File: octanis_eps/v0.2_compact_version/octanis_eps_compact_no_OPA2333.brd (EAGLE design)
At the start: 61.9 x 49.5 mm, 90 parts, among them IC3 OPA2333DGK, IC5 OPA2333DGK, IC6 OPA2333DGK, IC7 OPA2333DGK, IC9 OPA2333DGK, Q1 FC-12M, Q2 N-HEXFET-2D_SOT232-, Q3 N-HEXFET-2D_SOT232-, Q4 N-HEXFET-2D_SOT232-

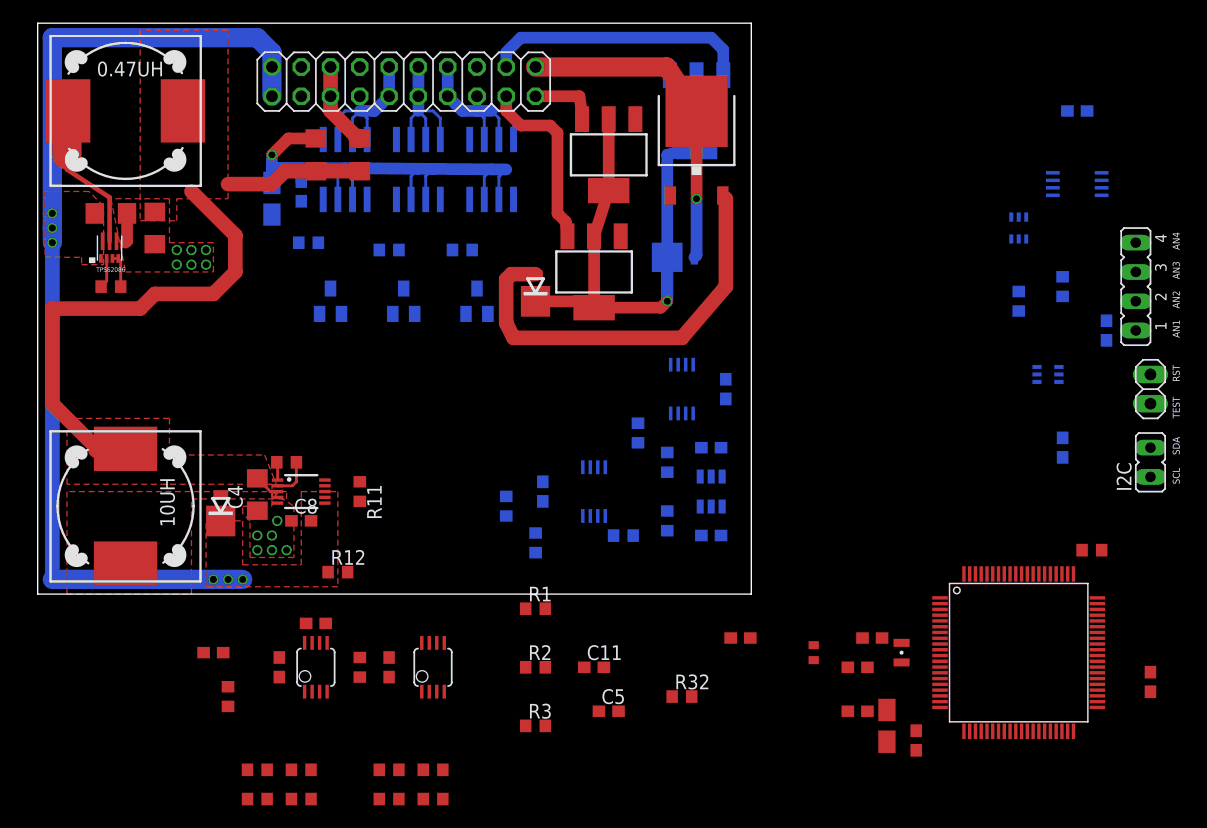
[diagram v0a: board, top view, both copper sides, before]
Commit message: compact version 5X6cm with MSP420Gxx24
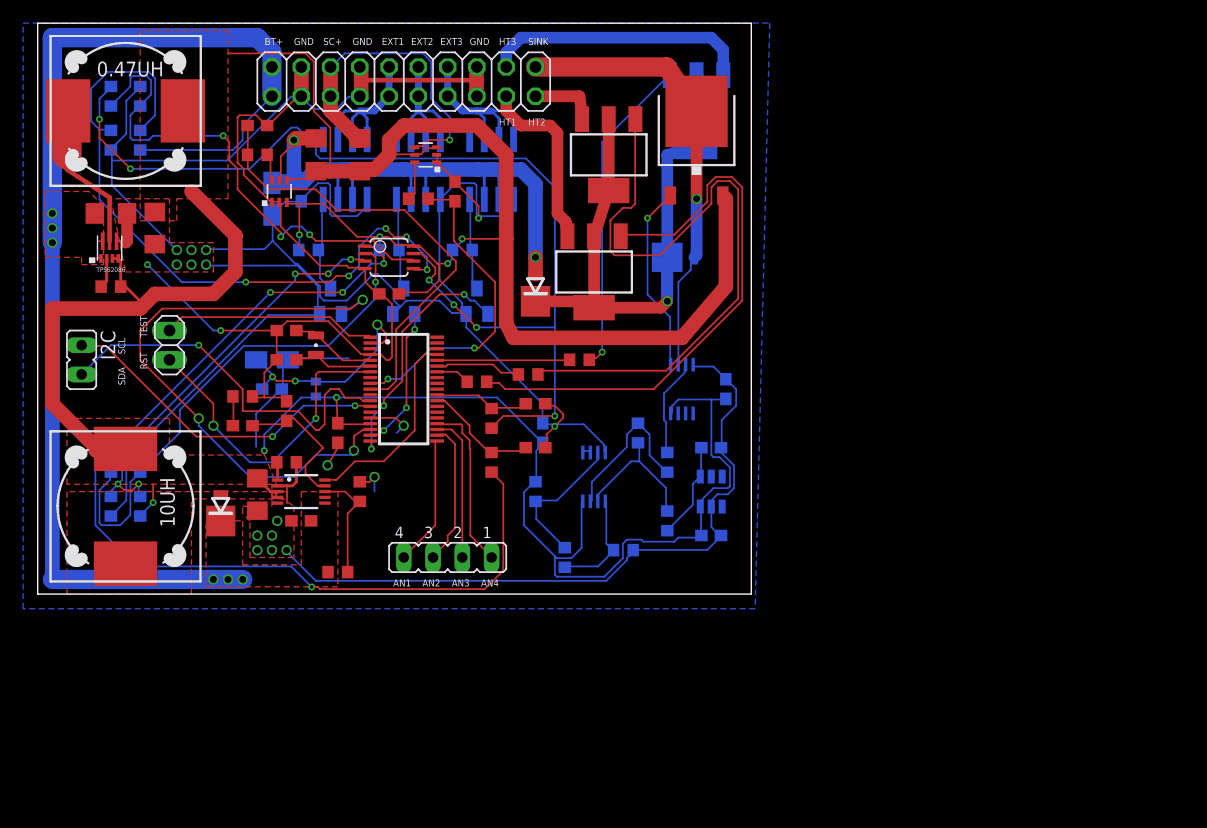
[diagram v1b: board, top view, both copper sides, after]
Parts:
- removed C20: 470nF, rcl:C0603
- removed C23, C_IC3, C_IC6: 100nF, rcl:C0603
- removed IC3, IC6: OPA2333DGK, linear:MSOP08
- removed R48: 1M, rcl:R0603
- removed U$1: F552X---PN80, TI_MSP430_v16:PN80
- added U$6: MSP430G2544, Octanis1_EPS:TSSOP38
- moved I2C 93.1 mm to (3.81, 50.8), turned to 180 degrees
- moved JP7 85.2 mm to (11.4, 52.1), turned to 90 degrees
- moved C2 75.8 mm to (19.1, 71.1), flipped to the top, turned to 180 degrees
- moved R7 67.3 mm to (19.1, 68.6), flipped to the top, turned to 0 degrees
- moved R22 64.7 mm to (8.89, 73.7), flipped to the bottom, turned to 90 degrees
- moved U$2 64.2 mm to (21.0, 65.4), flipped to the top, turned to 0 degrees
- moved A_EXT 64.1 mm to (35.6, 33.7), turned to 180 degrees
- moved R23 63.2 mm to (6.35, 73.7), flipped to the bottom, turned to 270 degrees
- moved R19 62.5 mm to (8.89, 69.8), flipped to the bottom, turned to 270 degrees
- moved C24 62.1 mm to (20.3, 50.8), flipped to the bottom, turned to 0 degrees
- moved R20 61.3 mm to (6.35, 69.8), flipped to the bottom, turned to 90 degrees
- moved C22 58.0 mm to (20.3, 48.3), flipped to the bottom
- moved C14 57.4 mm to (21.6, 53.3)
- moved Q1 57.4 mm to (24.1, 52.1)
- moved U$3 57.2 mm to (33.7, 68.6), flipped to the top
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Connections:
- removed net 65: U$1.65
- removed net 66: U$1.66
- removed net 67: U$1.67
- removed net AEXT4: A_EXT.1, U$1.80
- removed net N$11: C6.2, IC5.5, R16.1
- removed net N$27: R48.2, U$1.63
- removed net N$28: U$1.45
- removed net N$49: C20.1, U$1.20
- removed net N$6: C2.2, IC3.3, R7.1
- removed net N$7: C3.2, IC3.5, R9.1
- removed net N$9: C7.2, IC6.5, R21.1
- new net A_EXT4: A_EXT.1, U$6.23
- net +3V3: now also FERRITE_BEAD.1, U$6.2; no longer C21.2, C23.1, FERRITE_BEAD.2, U$1.14, U$1.18, U$1.50
- net A_EXT1: now also U$6.20; no longer U$1.77
- net A_EXT2: now also U$6.21; no longer U$1.78
- net A_EXT3: now also U$6.22; no longer U$1.79
- net EN_CHG: now also U$6.35; no longer U$1.29
- net EN_EXT1: now also U$6.17; no longer U$1.31
- net EN_EXT2: now also U$6.18; no longer U$1.32
- net EN_EXT3: now also U$6.19; no longer U$1.33
- net EN_HEAT1: now also U$6.32; no longer U$1.34
- net EN_HEAT2: now also U$6.33; no longer U$1.35
- net EN_HEAT3: now also U$6.34; no longer U$1.36
- net EXT_PW: now also U$8.A
- net GND: now also C21.1, U$6.15, U$6.4; no longer C20.2, C23.2, C_IC3.1, C_IC6.1, IC3.4, IC6.4, R48.1, U$1.19, U$1.49, U$1.61, U$1.68
- net I2C_SCL: now also U$6.13; no longer U$1.47
- net I2C_SDA: now also U$6.12; no longer U$1.46
- net I_EXT_PW: now also C2.2, R7.1, U$6.10; no longer IC3.1, IC3.2, U$1.6
- net I_SC: now also C3.2, R9.1, U$6.9; no longer IC3.6, IC3.7, U$1.5
- net N$10: now also IC5.7; no longer IC6.1
- net N$15: now also IC5.6; no longer IC6.2
- net N$16: now also IC5.5; no longer IC6.3
- net N$48: now also U$6.5; no longer U$1.12
- net N$50: now also U$6.6; no longer U$1.13
- net RST/SBWTDIO: now also U$6.7; no longer U$1.76
- net TEST/SBWTCK: now also U$6.1; no longer U$1.71
- net VCC: now also C21.2, FERRITE_BEAD.2, U$6.16; no longer C21.1, C_IC3.2, C_IC6.2, FERRITE_BEAD.1, IC3.8, IC6.8, U$1.11, U$8.A
- net V_BT_MS: now also C7.2, R21.1, U$6.28; no longer IC6.6, IC6.7, U$1.2
- net V_BUS_MS: now also C6.2, R16.1, U$6.27; no longer IC5.6, IC5.7, U$1.1
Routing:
- net GND: track 6.06 -> 363.5 mm, vias 12 -> 19
- net VCC: track 95.6 -> 266.4 mm, vias 0 -> 7
- net N$10: track 0.00 -> 91.6 mm, vias 0 -> 6
- net N$12: track 0.00 -> 87.3 mm, vias 0 -> 4
- net N$16: track 0.00 -> 59.9 mm, vias 0 -> 5
- net N$31: track 0.00 -> 57.5 mm
- net EN_EXT1: track 0.00 -> 52.2 mm, vias 0 -> 3
- net N$29: track 0.00 -> 49.5 mm
- net N$13: track 0.00 -> 44.5 mm, vias 0 -> 1
- net N$15: track 0.00 -> 43.1 mm, vias 0 -> 3
- net I_EXT_PW: track 0.00 -> 40.2 mm
- net N$14: track 0.00 -> 36.0 mm, vias 0 -> 5
- net I2C_SDA: track 0.00 -> 33.8 mm, vias 0 -> 1
- net I2C_SCL: track 0.00 -> 29.4 mm, vias 0 -> 2
- net I_SC: track 0.00 -> 27.9 mm, vias 0 -> 2
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- added copper zone on layer 16, net GND
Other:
- board text added: "BT+"
- board text added: "EXT1"
- board text added: "EXT2"
- board text added: "EXT3"
- board text added: "GND"
- board text added: "HT1"
- board text added: "HT2"
- board text added: "HT3"
- board text added: "SC+"
- board text added: "SINK"

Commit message: correction & redesign on of the boost converter running
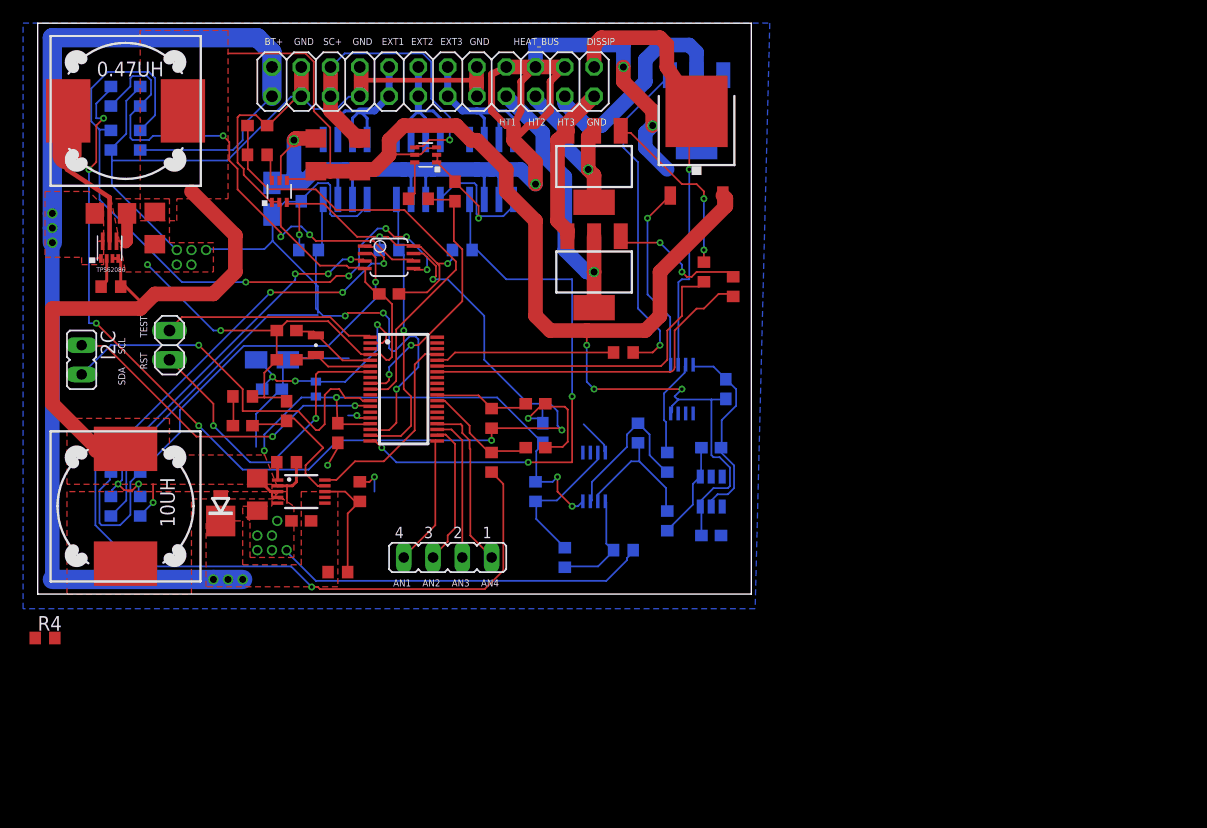
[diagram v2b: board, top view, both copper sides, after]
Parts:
- removed U$13, U$14, U$15: FDV301N, Octanis1_EPS:SOT23
- removed U$8, U$9: MBRM120LTIG, Octanis1_EPS:DO216AA
- added R4: 100k, rcl:R0603
- C2, C3, C6, C7: value 150nF -> 1.5uF
- JP1: device pinhead:2X10 -> pinhead:2X12
- R11: value 549k -> 50k
- R12: value 1.3M -> 286k
- R16, R21, R7, R9: value 10k -> 1k
- moved R1 23.7 mm to (60.3, 57.1), turned to 270 degrees
- moved R2 17.6 mm to (57.8, 58.4), turned to 270 degrees
- moved R3 3.86 mm to (50.8, 51.4)
- moved JP1 2.54 mm to (34.3, 74.9)
- moved Q3 1.63 mm to (48.3, 67.6)
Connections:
- removed net N$17: IC7.1, IC7.2
- removed net N$34: R80.2, U$15.3, U$17.4
- removed net N$79: R81.2, U$13.3, U$16.4
- removed net N$80: R79.2, U$14.3, U$18.4
- net DISSIP: now also JP1.24; no longer JP1.20, U$9.A
- net EN_EXT1: now also R81.2, U$16.4; no longer U$13.1
- net EN_EXT2: now also R80.2, U$17.4; no longer U$15.1
- net EN_EXT3: now also R79.2, U$18.4; no longer U$14.1
- net EXT_PW: now also JP1.18, JP1.20, JP1.22; no longer U$8.A
- net GND: now also JP1.23, Q2.3, Q3.3, Q4.3; no longer U$13.2, U$14.2, U$15.2
- net HEAT1: now also Q2.2, Q2.4; no longer Q2.3
- net HEAT2: now also Q3.2, Q3.4; no longer Q3.3
- net HEAT3: now also JP1.21, Q4.2, Q4.4; no longer JP1.18, Q4.3
- net N$18: no longer IC7.3
- net N$23: now also R4.1
- net N$5: now also R4.2; no longer Q2.2, Q2.4, Q3.2, Q3.4, Q4.2, Q4.4, U$8.C, U$9.C
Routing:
- net N$5: track 53.8 -> 0.00 mm, vias 1 -> 0
- net GND: track 363.5 -> 315.1 mm, vias 19 -> 18
- net EXT_PW: track 58.7 -> 105.6 mm, vias 2 -> 4
- net N$31: track 57.5 -> 15.5 mm, vias 0 -> 2
- net N$29: track 49.5 -> 11.9 mm, vias 0 -> 2
- net EN_HEAT1: track 2.96 -> 30.4 mm
- net EN_EXT3: track 21.6 -> 48.4 mm
- net VCC: track 266.4 -> 244.6 mm, vias 7 -> 11
- net EN_HEAT2: track 7.55 -> 29.1 mm
- net EN_EXT1: track 52.2 -> 33.1 mm
- net EN_EXT2: track 12.6 -> 24.1 mm, vias 3 -> 1
- net HEAT1: track 15.8 -> 25.0 mm, vias 0 -> 1
- net HEAT2: track 5.81 -> 14.9 mm, vias 0 -> 1
- net N$79: track 8.42 -> 0.00 mm
- net N$34: track 8.12 -> 0.00 mm
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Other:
- board text added: "DISSIP"
- board text added: "HEAT_BUS"
- board text removed: "SINK"

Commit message: completed FeedBack loop regulation on charge circuit & routing
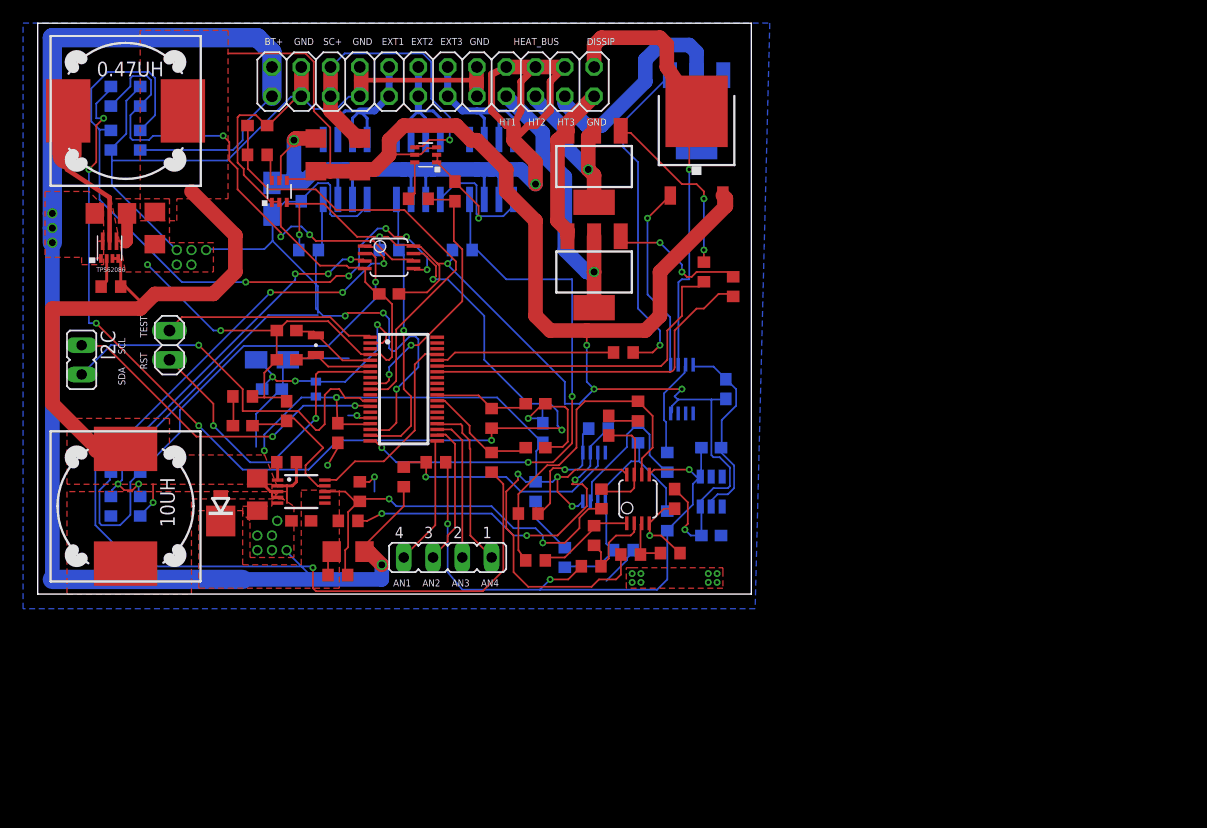
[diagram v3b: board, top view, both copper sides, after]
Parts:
- added C1: 10nF, rcl:C0603
- added C_IC1: 100nF, rcl:C0603
- added IC1: OPA2333DGK, linear:MSOP08
- added R30: 20k, rcl:R0603
- added R31: 23.2k, rcl:R0603
- added R33: 1M, rcl:R0603
- added R34, R35, R36: 162k, rcl:R0603
- added R37: 50m, rcl:R1206
- added R38, R39: 10k, rcl:R0603
- added R40, R41: 920k, rcl:R0603
- added R5: 31.60k, rcl:R0603
- R11: value 50k -> 100k
- R12: value 286k -> 200k
- R4: value 100k -> 560k
- moved R4 49.7 mm to (48.9, 38.7), turned to 90 degrees
- moved R12 0.25 mm to (26.0, 32.1)
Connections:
- new net BT_CHG: C8.2, R12.1, R37.2, R38.1, U$10.C, U$4.7
- new net CHG_CMD: C1.1, IC1.7, R4.2
- new net N$11: IC1.6, R34.1, R35.2, R36.2
- new net N$17: IC7.2, R38.2, R41.1
- new net N$27: C1.2, R34.2
- new net N$28: IC7.3, R39.2, R40.1
- new net N$6: IC1.3, R30.1, R5.2
- new net N$7: IC1.2, R31.1, R33.1
- new net N$9: IC1.1, R33.2, R35.1
- net BT+: now also R37.1, R39.1; no longer C8.2, R12.1, U$10.C, U$4.7
- net GND: now also C_IC1.1, IC1.4, R30.2
- net N$5: now also IC7.1, R36.1, R41.2; no longer R4.2
- net VCC: now also C_IC1.2, IC1.8, R5.1
- net VREF: now also IC1.5, R31.2, R40.2
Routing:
- net VCC: track 244.6 -> 299.3 mm, vias 11 -> 13
- net VREF: track 8.41 -> 51.7 mm, vias 0 -> 3
- net N$17: track 0.00 -> 30.9 mm, vias 0 -> 3
- net N$11: track 0.00 -> 28.9 mm
- net GND: track 315.1 -> 287.6 mm, vias 18 -> 27
- net N$23: track 9.95 -> 35.2 mm, vias 0 -> 2
- net EXT_PW: track 105.6 -> 83.1 mm, vias 4 -> 2
- net BT+: track 104.4 -> 126.8 mm, vias 6 -> 4
- net N$28: track 0.00 -> 20.9 mm, vias 0 -> 1
- net N$5: track 0.00 -> 10.7 mm, vias 0 -> 1
- net CHG_CMD: track 0.00 -> 9.77 mm
- net N$9: track 0.00 -> 8.52 mm
- net N$7: track 0.00 -> 7.73 mm
- net N$18: track 12.5 -> 5.06 mm
- net N$6: track 0.00 -> 4.51 mm
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- added copper zone on layer 1, net BT_CHG
